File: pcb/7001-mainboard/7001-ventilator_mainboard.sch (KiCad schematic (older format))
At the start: 118 parts, among them J1 USB_B_Micro, J10 6-pin header, J11 4-pin screw terminal, J12 3-pin screw terminal, J13 2-pin screw terminal, J14 2-pin screw terminal, J15 6-pin header, J2 4-pin header, J3 2-pin screw terminal, J4 DNI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

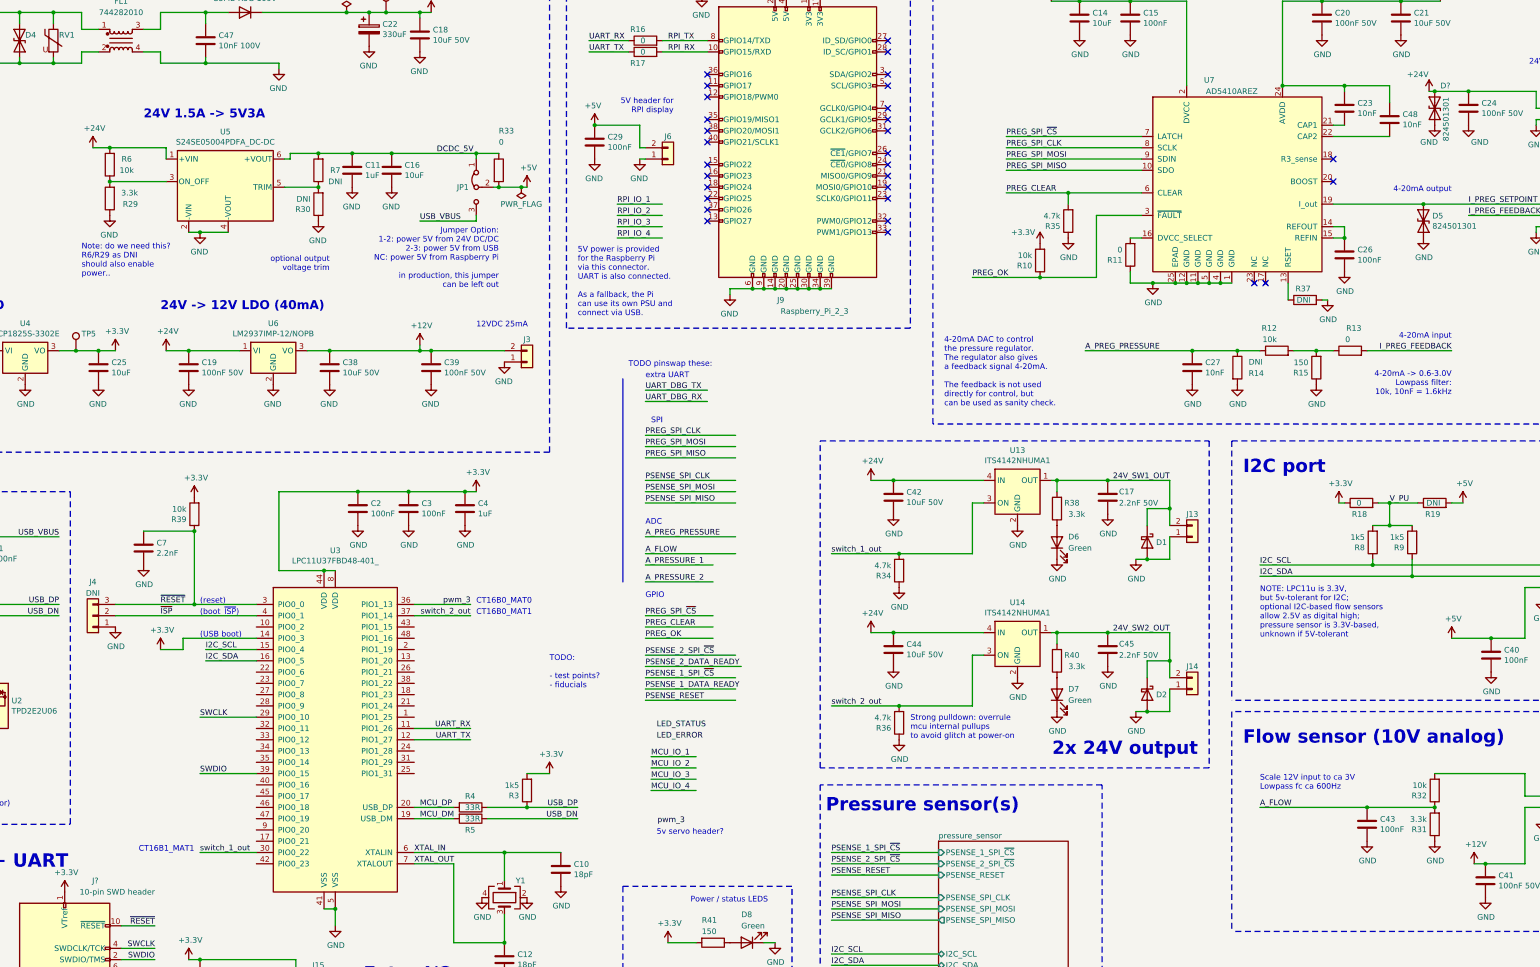
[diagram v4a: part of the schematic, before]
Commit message: Sync design with BOM
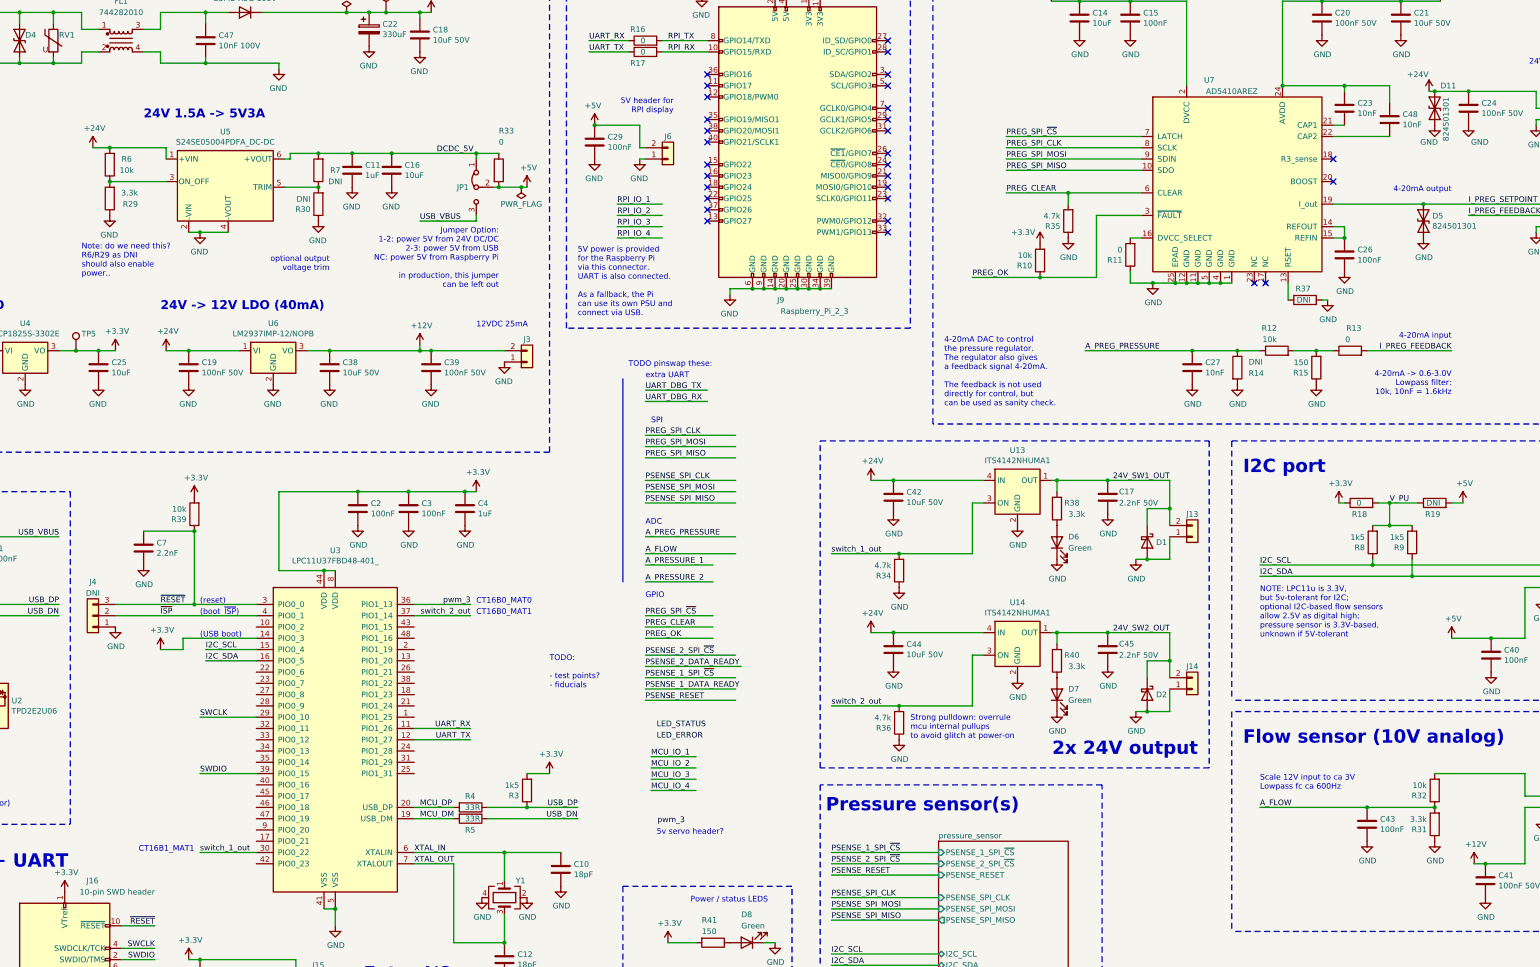
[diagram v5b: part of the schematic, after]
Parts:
- J15: value 6-pin header -> 2x10-pin header; MPN (none) -> 61032021121
- gave numbers to parts that had none: 2
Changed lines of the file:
@@
 AR Path="/5EDC7103" Ref="J15"  Part="1"
 F 0 "J15" H 4850 9850 50  0000 C CNN
-F 1 "6-pin header" H 4800 10150 50  0001 C CNN
+F 1 "2x10-pin header" H 4800 10150 50  0001 C CNN
 F 2 "Connector_PinHeader_2.54mm:PinHeader_2x10_P2.54mm_Vertical_SMD" H 4750 10450 50  0001 C CNN
 F 3 "~" H 4750 10450 50  0001 C CNN
+F 4 "61032021121" H 4750 10450 50  0001 C CNN "MPN"
 	1    4750 10450
 	-1   0    0    1
@@
 $EndComp
 $Comp
-L Device:D_TVS D?
+L Device:D_TVS D11
 U 1 1 5F60AF83
 P 14550 2250
-F 0 "D?" V 14750 2200 50  0000 R CNN
+F 0 "D11" V 14750 2200 50  0000 R CNN
 F 1 "D_TVS" V 14505 2171 50  0001 R CNN
 F 2 "" H 14550 2250 50  0001 C CNN
@@
 P 14550 2400
 AR Path="/5BF2E340/5F60AF89" Ref="#PWR?"  Part="1"
-AR Path="/5F60AF89" Ref="#PWR?"  Part="1"
-F 0 "#PWR?" H 14550 2150 50  0001 C CNN
+AR Path="/5F60AF89" Ref="#PWR0145"  Part="1"
+F 0 "#PWR0145" H 14550 2150 50  0001 C CNN
 F 1 "GND" H 14500 2250 50  0000 C CNN
 F 2 "" H 14550 2400 50  0001 C CNN
@@
 PSENSE_RESET
 $Comp
-L Connector:Conn_ARM_JTAG_SWD_10 J?
+L Connector:Conn_ARM_JTAG_SWD_10 J16
 U 1 1 5F70729E
 P 2400 9800
-F 0 "J?" H 2700 10500 50  0000 R CNN
+F 0 "J16" H 2700 10500 50  0000 R CNN
 F 1 "10-pin SWD header" H 3200 10400 50  0000 R CNN
 F 2 "Jitter_Footprints:connector_jtag_10pin_shrouded" H 2400 9800 50  0001 C CNN
@@
 Connection ~ 3500 10650
 $Comp
-L power:+3.3V #PWR?
+L power:+3.3V #PWR0154
 U 1 1 5F811EBF
 P 900 9400
-F 0 "#PWR?" H 900 9250 50  0001 C CNN
+F 0 "#PWR0154" H 900 9250 50  0001 C CNN
 F 1 "+3.3V" H 915 9573 50  0000 C CNN
 F 2 "" H 900 9400 50  0001 C CNN
@@
 $EndComp
 $Comp
-L power:+3.3V #PWR?
+L power:+3.3V #PWR0189
 U 1 1 5F8123D3
 P 2400 9200
-F 0 "#PWR?" H 2400 9050 50  0001 C CNN
+F 0 "#PWR0189" H 2400 9050 50  0001 C CNN
 F 1 "+3.3V" H 2415 9373 50  0000 C CNN
 F 2 "" H 2400 9200 50  0001 C CNN
@@
 P 2500 10400
 AR Path="/5BF2E340/5F91C9B4" Ref="#PWR?"  Part="1"
-AR Path="/5F91C9B4" Ref="#PWR?"  Part="1"
-F 0 "#PWR?" H 2500 10150 50  0001 C CNN
+AR Path="/5F91C9B4" Ref="#PWR0190"  Part="1"
+F 0 "#PWR0190" H 2500 10150 50  0001 C CNN
 F 1 "GND" H 2505 10227 50  0000 C CNN
 F 2 "" H 2500 10400 50  0001 C CNN

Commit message: Finalize BOM, add all footprints
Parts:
- D11, D4, D5: footprint (none) -> Jitter_Footprints:WE-TVSP_TVS_DIODE; Farnell (none) -> 2536572
- D3: footprint (none) -> Diode_SMD:D_SMB
- FL1: footprint (none) -> Jitter_Footprints:L_CommonMode_Wuerth_WE-SCC
- J9: footprint (none) -> Jitter_Footprints:PinSocket_2x20_P2.54mm_Vertical_holes_SMD; Farnell 2827937 -> (none); MPN 610020243021 -> REF-182665-01; mates with (none) -> REF-182683-02
- RV1: footprint (none) -> Jitter_Footprints:WE_VS_Varistor
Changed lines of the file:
@@
 F 0 "J9" H 8750 1150 50  0000 C CNN
 F 1 "Raspberry_Pi_2_3" H 9050 1050 50  0000 C CNN
-F 2 "" H 8900 2550 50  0001 C CNN
+F 2 "Jitter_Footprints:PinSocket_2x20_P2.54mm_Vertical_holes_SMD" H 8900 2550 50  0001 C CNN
 F 3 "https://github.com/raspberrypi/hats/blob/master/hat-board-mechanical.pdf" H 8900 2550 50  0001 C CNN
-F 4 "610020243021" H 8900 2550 50  0001 C CNN "MPN"
-F 5 "2827937" H 8900 2550 50  0001 C CNN "Farnell"
+F 4 "REF-182665-01" H 8900 2550 50  0001 C CNN "MPN"
+F 5 "REF-182683-02" H 8900 2550 50  0001 C CNN "mates with"
 	1    8900 2550
 	1    0    0    -1
@@
 F 0 "D3" H 4000 1184 50  0000 C CNN
 F 1 "S5MB R5G 100V" H 4000 1275 50  0000 C CNN
-F 2 "" H 4000 1400 50  0001 C CNN
+F 2 "Diode_SMD:D_SMB" H 4000 1400 50  0001 C CNN
 F 3 "~" H 4000 1400 50  0001 C CNN
 F 4 "S5MB R5G" H 4000 1400 50  0001 C CNN "MPN"
@@
 F 0 "D4" V 2050 1600 50  0000 R CNN
 F 1 "D_TVS" V 1955 1571 50  0001 R CNN
-F 2 "" H 2000 1650 50  0001 C CNN
+F 2 "Jitter_Footprints:WE-TVSP_TVS_DIODE" H 2000 1650 50  0001 C CNN
 F 3 "~" H 2000 1650 50  0001 C CNN
 F 4 "824501301" H 2250 1550 50  0001 R CNN "MPN"
+F 5 "2536572" V 2000 1650 50  0001 C CNN "Farnell"
 	1    2000 1650
 	0    -1   -1   0
-$EndComp
-$Comp
-L Jitter_Components:CommonModeChoke_744282010 FL1
-U 1 1 5F29E98E
-P 2900 1650
-F 0 "FL1" H 2900 2000 50  0000 C CNN
-F 1 "744282010" H 2900 1900 50  0000 C CNN
-F 2 "" H 2900 1690 50  0001 C CNN
-F 3 "~" H 2900 1690 50  0001 C CNN
-F 4 "744282010" H 2900 1840 50  0001 C CNN "MPN"
-	1    2900 1650
-	1    0    0    -1
 $EndComp
 Wire Wire Line
@@
 F 0 "RV1" H 2350 1700 50  0000 L CNN
 F 1 "Varistor" H 2403 1605 50  0001 L CNN
-F 2 "" V 2230 1650 50  0001 C CNN
+F 2 "Jitter_Footprints:WE_VS_Varistor" V 2230 1650 50  0001 C CNN
 F 3 "~" H 2300 1650 50  0001 C CNN
 F 4 "82551250" H 2300 1650 50  0001 C CNN "MPN"
@@
 F 0 "D5" V 14496 3171 50  0000 R CNN
 F 1 "D_TVS" V 14405 3171 50  0001 R CNN
-F 2 "" H 14450 3250 50  0001 C CNN
+F 2 "Jitter_Footprints:WE-TVSP_TVS_DIODE" H 14450 3250 50  0001 C CNN
 F 3 "~" H 14450 3250 50  0001 C CNN
 F 4 "824501301" V 14405 3171 50  0000 R CNN "MPN"
+F 5 "2536572" V 14450 3250 50  0001 C CNN "Farnell"
 	1    14450 3250
 	0    -1   -1   0
@@
 F 0 "D11" V 14750 2200 50  0000 R CNN
 F 1 "D_TVS" V 14505 2171 50  0001 R CNN
-F 2 "" H 14550 2250 50  0001 C CNN
+F 2 "Jitter_Footprints:WE-TVSP_TVS_DIODE" H 14550 2250 50  0001 C CNN
 F 3 "~" H 14550 2250 50  0001 C CNN
 F 4 "824501301" H 14650 2150 50  0000 R CNN "MPN"
+F 5 "2536572" V 14550 2250 50  0001 C CNN "Farnell"
 	1    14550 2250
 	0    -1   -1   0
@@
 Wire Wire Line
 	2400 10400 2300 10400
+$Comp
+L Jitter_Components:CommonModeChoke_744282010 FL1
+U 1 1 5F9AA62A
+P 2900 1650
+F 0 "FL1" H 2900 1931 50  0000 C CNN
+F 1 "744282010" H 2900 1840 50  0000 C CNN
+F 2 "Jitter_Footprints:L_CommonMode_Wuerth_WE-SCC" H 2900 1690 50  0001 C CNN
+F 3 "~" H 2900 1690 50  0001 C CNN
+F 4 "744282010" H 2900 1839 50  0001 C CNN "MPN"
+	1    2900 1650
+	1    0    0    -1
+$EndComp
 $EndSCHEMATC

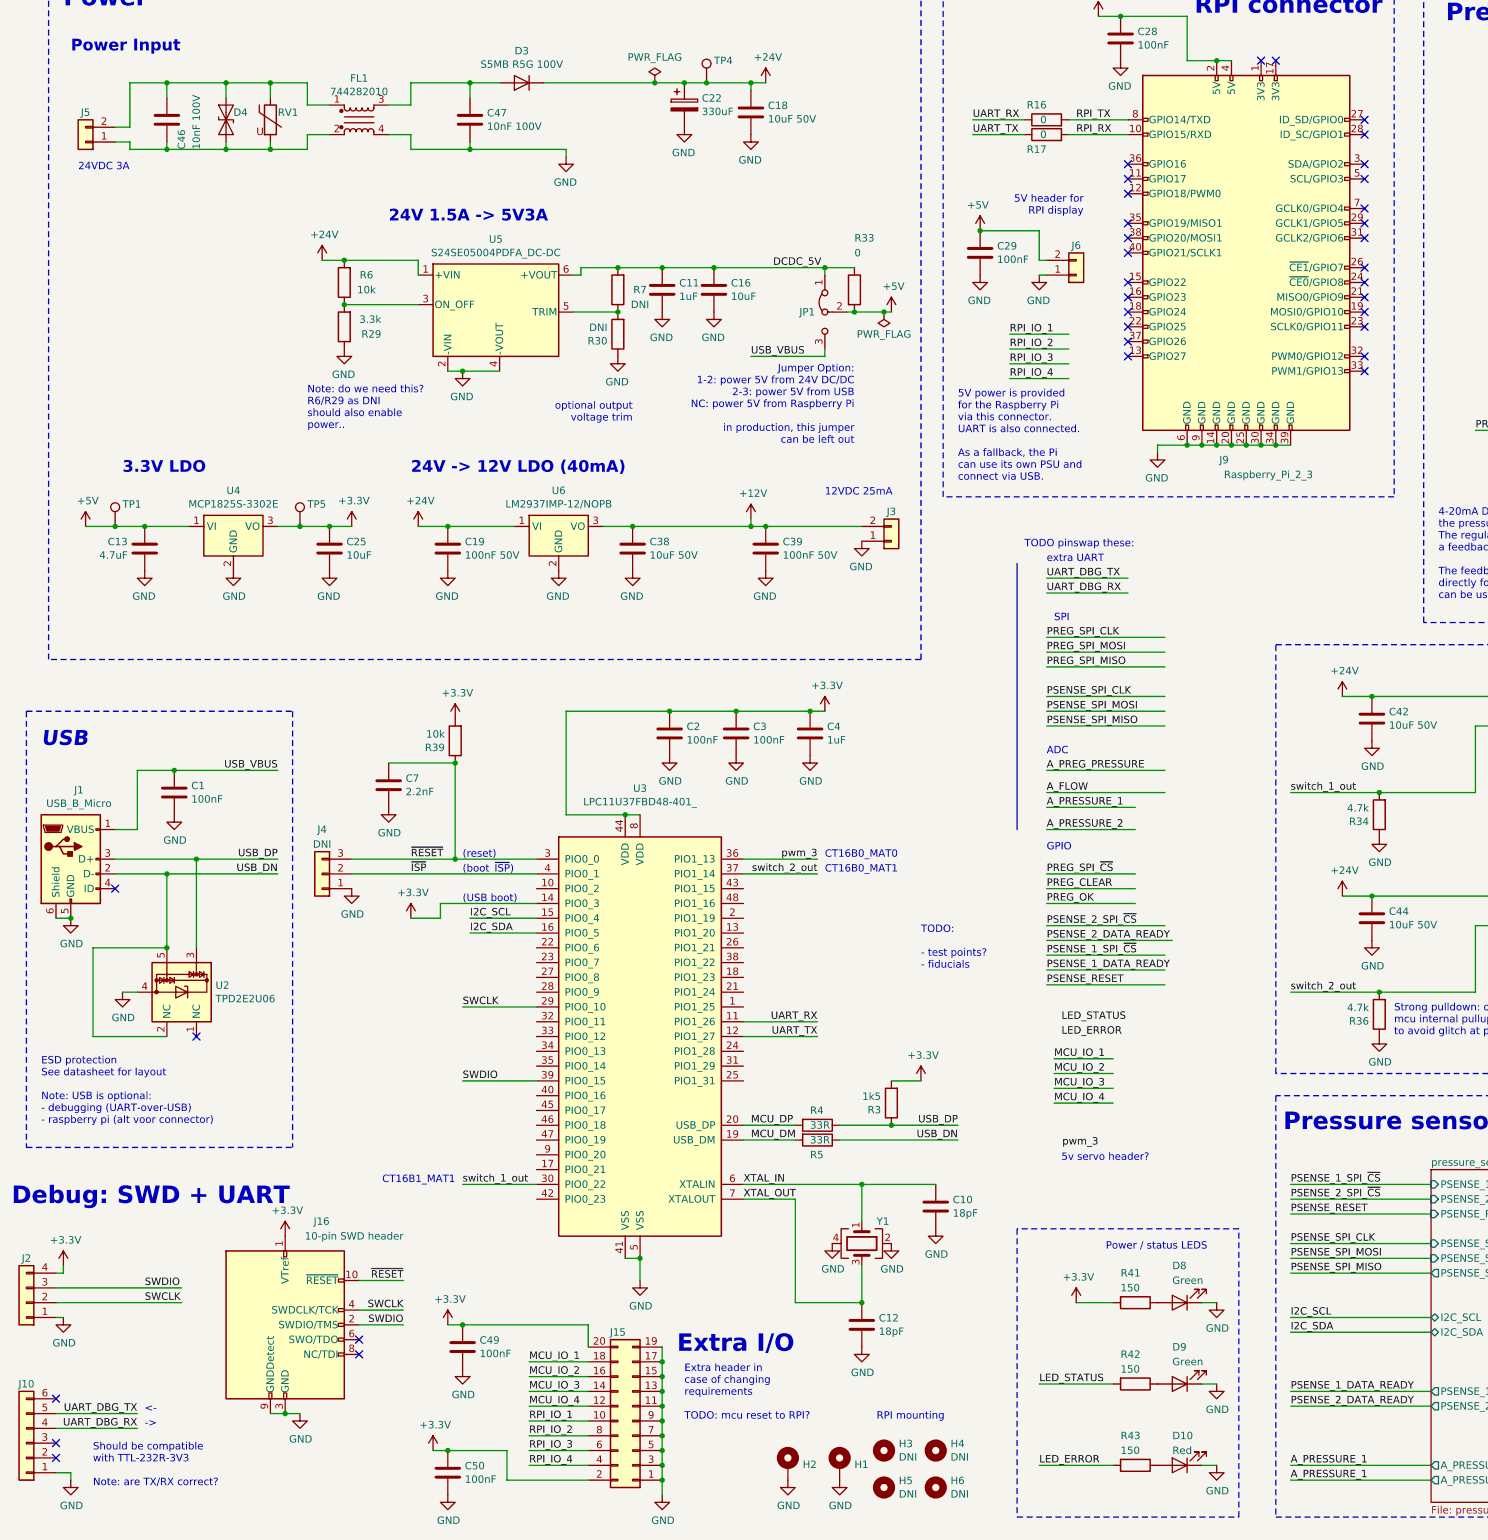
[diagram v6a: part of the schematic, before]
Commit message: PCB: Halfway layouting
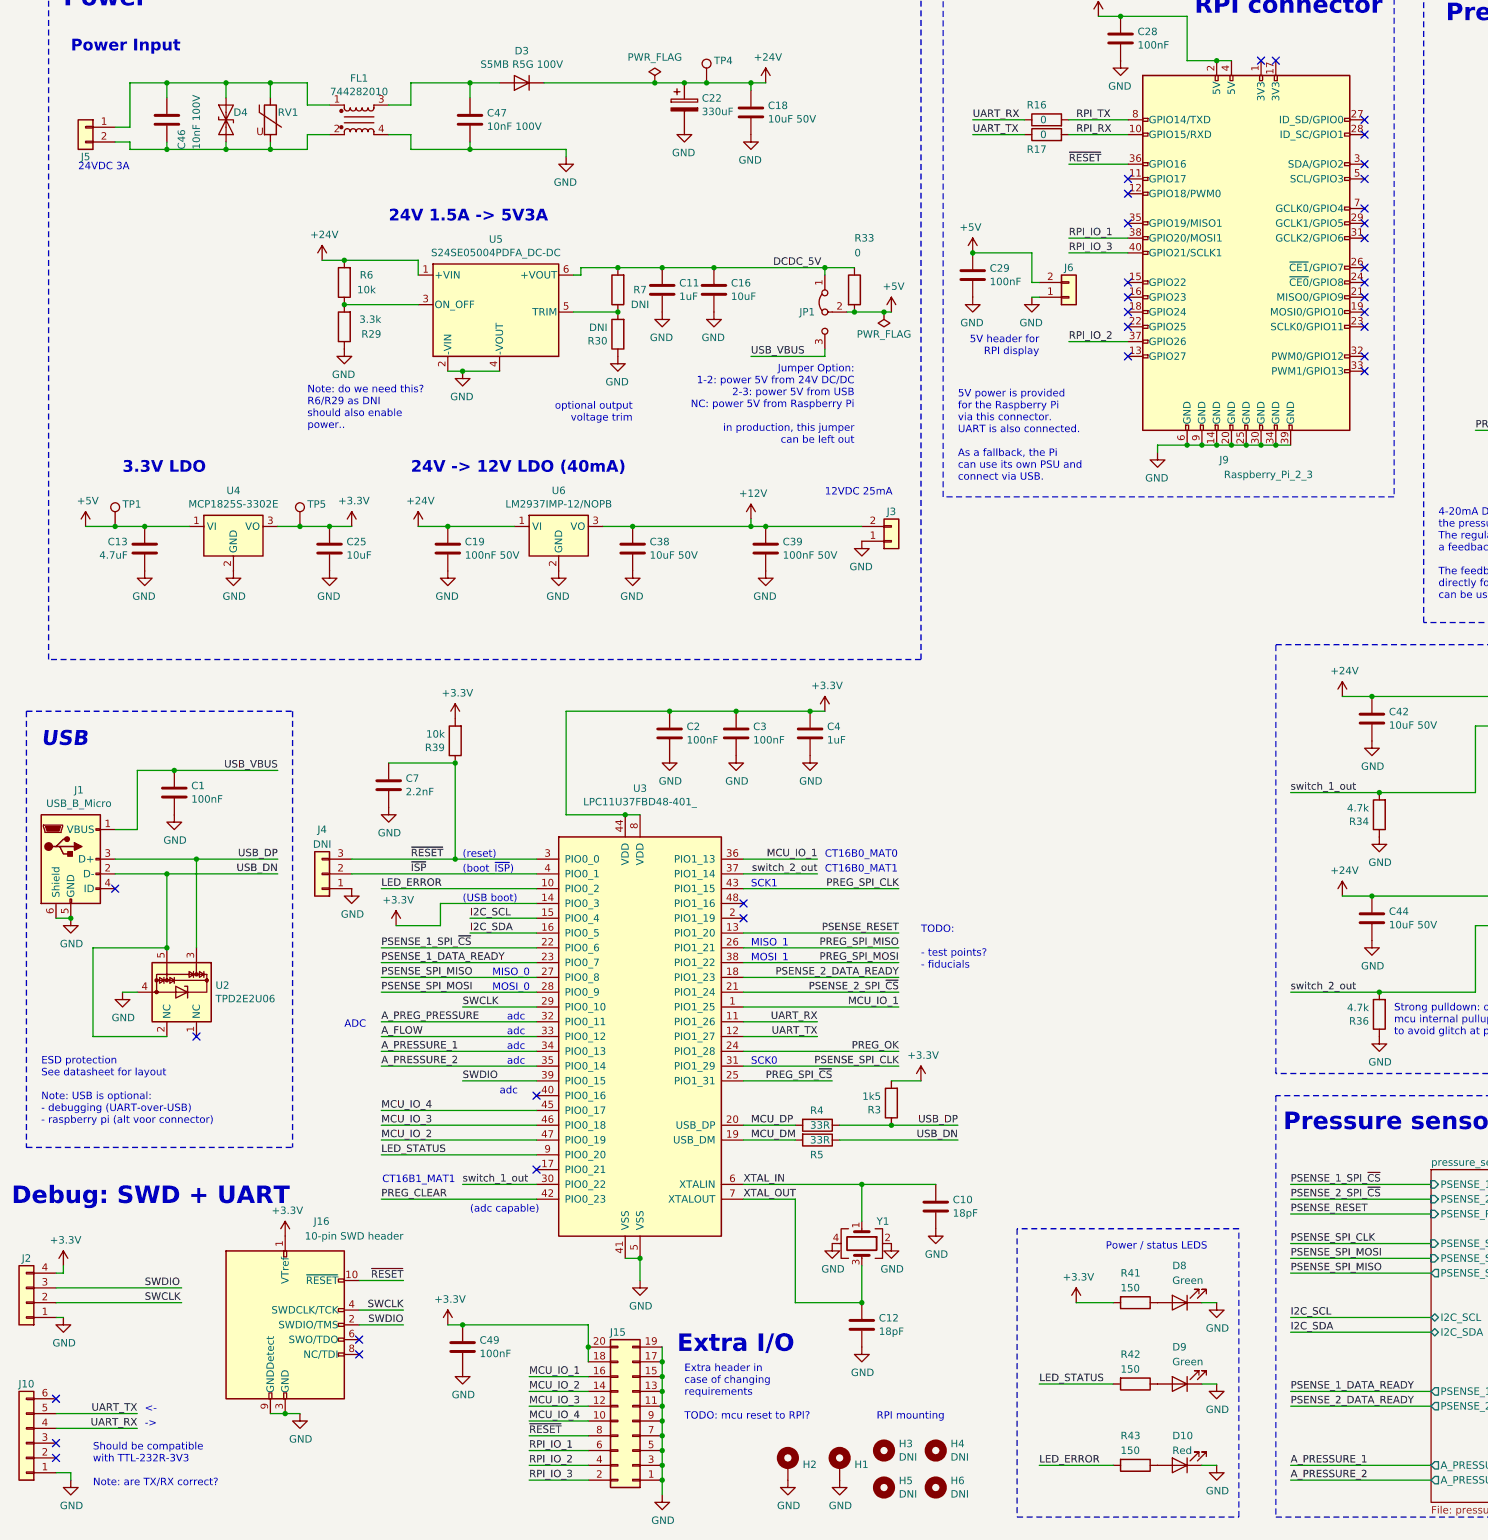
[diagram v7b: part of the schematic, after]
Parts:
- removed C50: 100nF, Capacitor_SMD:C_0805_2012Metric, symbol Device:C
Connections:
- net labels removed: RPI_IO_4, UART_DBG_RX, UART_DBG_TX, pwm_3
- wire segments 350 -> 347
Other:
- note added: "(adc capable)"
- note added: "MISO_0"
- note added: "MISO_1"
- note added: "MOSI_0"
- note added: "MOSI_1"
- note added: "SCK0"
- note added: "SCK1"
- note added: "adc"
- note removed: "5v servo header?"
- note removed: "GPIO"
- note removed: "SPI"
- note removed: "TODO pinswap these:"
- note removed: "extra UART"
- moved on the sheet: C29, J6
